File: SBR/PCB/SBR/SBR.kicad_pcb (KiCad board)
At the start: 2 copper layers, 50 x 100 mm, 12 parts, among them J1 12V Input, J2 MOTOR_A, J3 MOTOR_B, M1 MPU6050, M2 HC-05, U1 LM7805

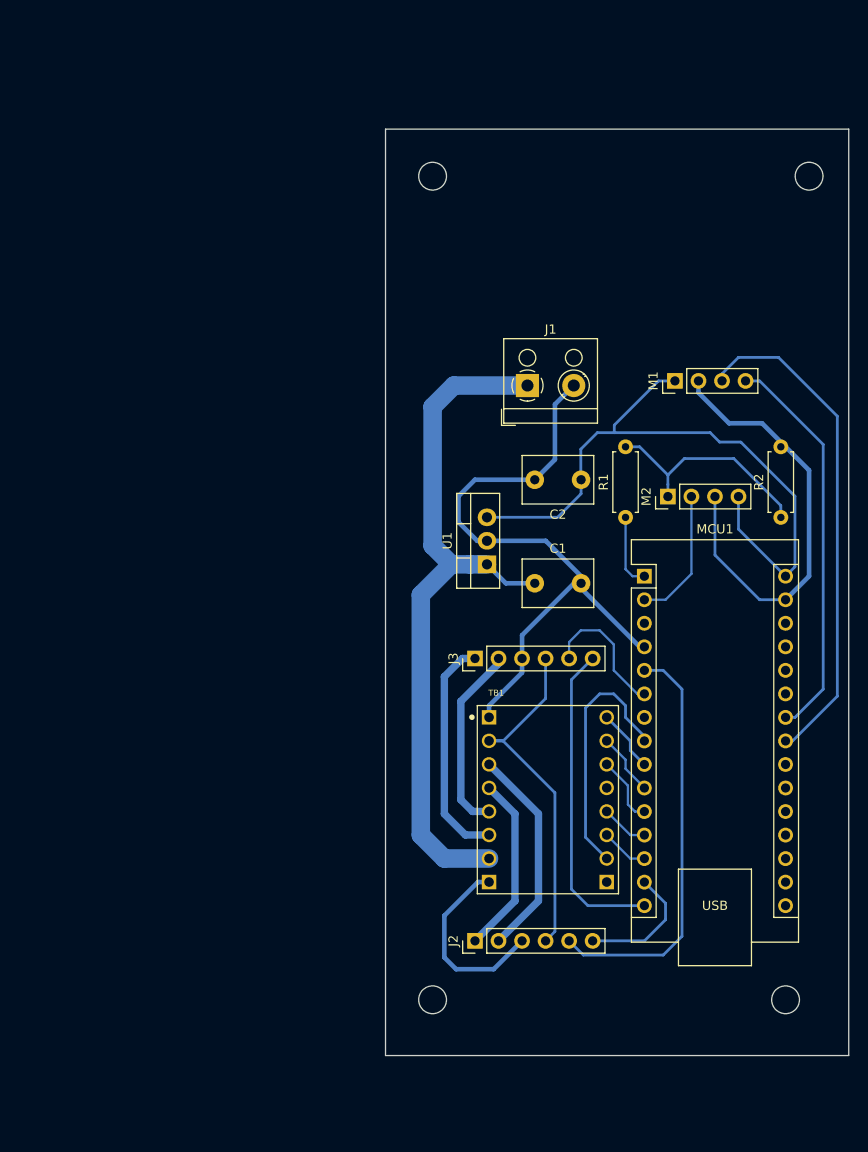
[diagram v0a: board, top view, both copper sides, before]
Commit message: Added copper fill to PCB, and made small design changes.
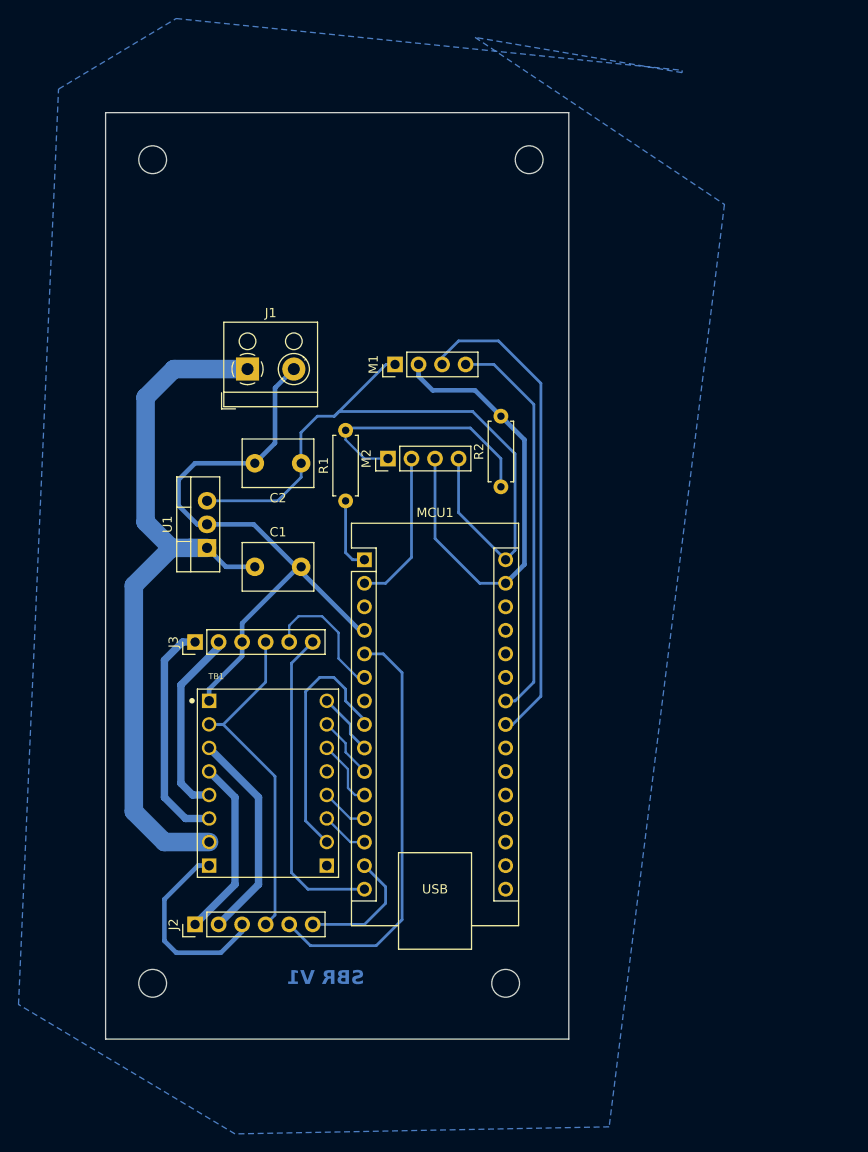
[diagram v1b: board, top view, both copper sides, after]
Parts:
- moved M2 30.5 mm to (58.7, 66.0)
- moved R2 30.4 mm to (70.9, 69.1)
- moved M1 30.3 mm to (59.4, 55.9)
- moved C1 30.3 mm to (44.3, 77.7)
- moved C2 30.3 mm to (49.3, 66.5)
- moved J2 30.3 mm to (37.9, 116.3)
- moved J3 30.3 mm to (37.9, 85.8)
- moved MCU1 30.3 mm to (56.1, 77.0)
- moved R1 30.3 mm to (54.1, 70.6)
- moved TB1 30.3 mm to (45.7, 101.1)
- moved U1 30.3 mm to (39.2, 75.7)
- moved J1 30.3 mm to (43.5, 56.4)
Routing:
- net /5V MCU: track 110.2 -> 113.9 mm
- net Net-(M2-Pin_1): track 24.5 -> 27.7 mm
- net /D1: track 14.6 -> 16.9 mm
- net GND: track 137.8 -> 139.7 mm
- net /SDA: track 54.4 -> 52.9 mm
- net /12V: track 79.0 -> 80.3 mm
- net /MA_ENCA: track 45.9 -> 46.5 mm
- added copper zone on B.Cu, net GND
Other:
- board text added: "SBR V1"

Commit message: Added robotic arm CAD files.
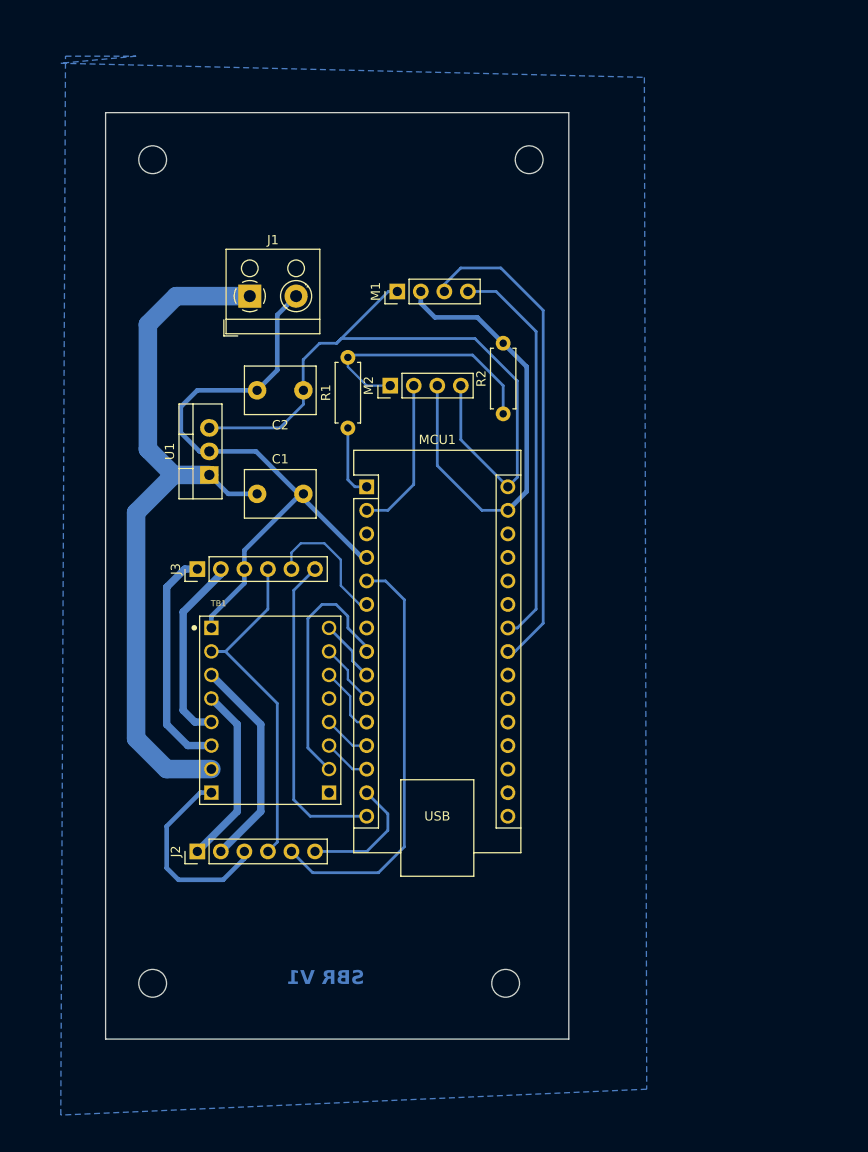
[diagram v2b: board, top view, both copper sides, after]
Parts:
- moved C1 7.88 mm to (44.6, 69.8)
- moved J2 7.88 mm to (38.1, 108.4)
- moved M2 7.88 mm to (58.9, 58.2)
- moved MCU1 7.88 mm to (56.4, 69.1)
- moved C2 7.88 mm to (49.6, 58.7)
- moved J1 7.88 mm to (43.8, 48.5)
- moved M1 7.88 mm to (59.7, 48.0)
- moved J3 7.88 mm to (38.1, 78.0)
- moved R1 7.88 mm to (54.4, 62.7)
- moved R2 7.88 mm to (71.1, 61.2)
- moved TB1 7.88 mm to (46.0, 93.2)
- moved U1 7.88 mm to (39.4, 67.8)
